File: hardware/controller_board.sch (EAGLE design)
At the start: 136 parts, among them J1 FRSKY-GIMBAL-FRYSKY, J11 USB-MICROA-AMPHENOL-10118192-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, J2 FRSKY-GIMBAL-FRYSKY, J3 USB-MINIB-EDAC-690-005-299-043, J4 AVR_SPI_PRG_6NS, J5 JUMPER-SMT_2_NC_PASTE_NO-SILK, J8 FRSKY-GIMBAL-2X-SERVO, J9 FRSKY-GIMBAL-2X-SERVO, P1 TEST-POINT, P2 TEST-POINT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

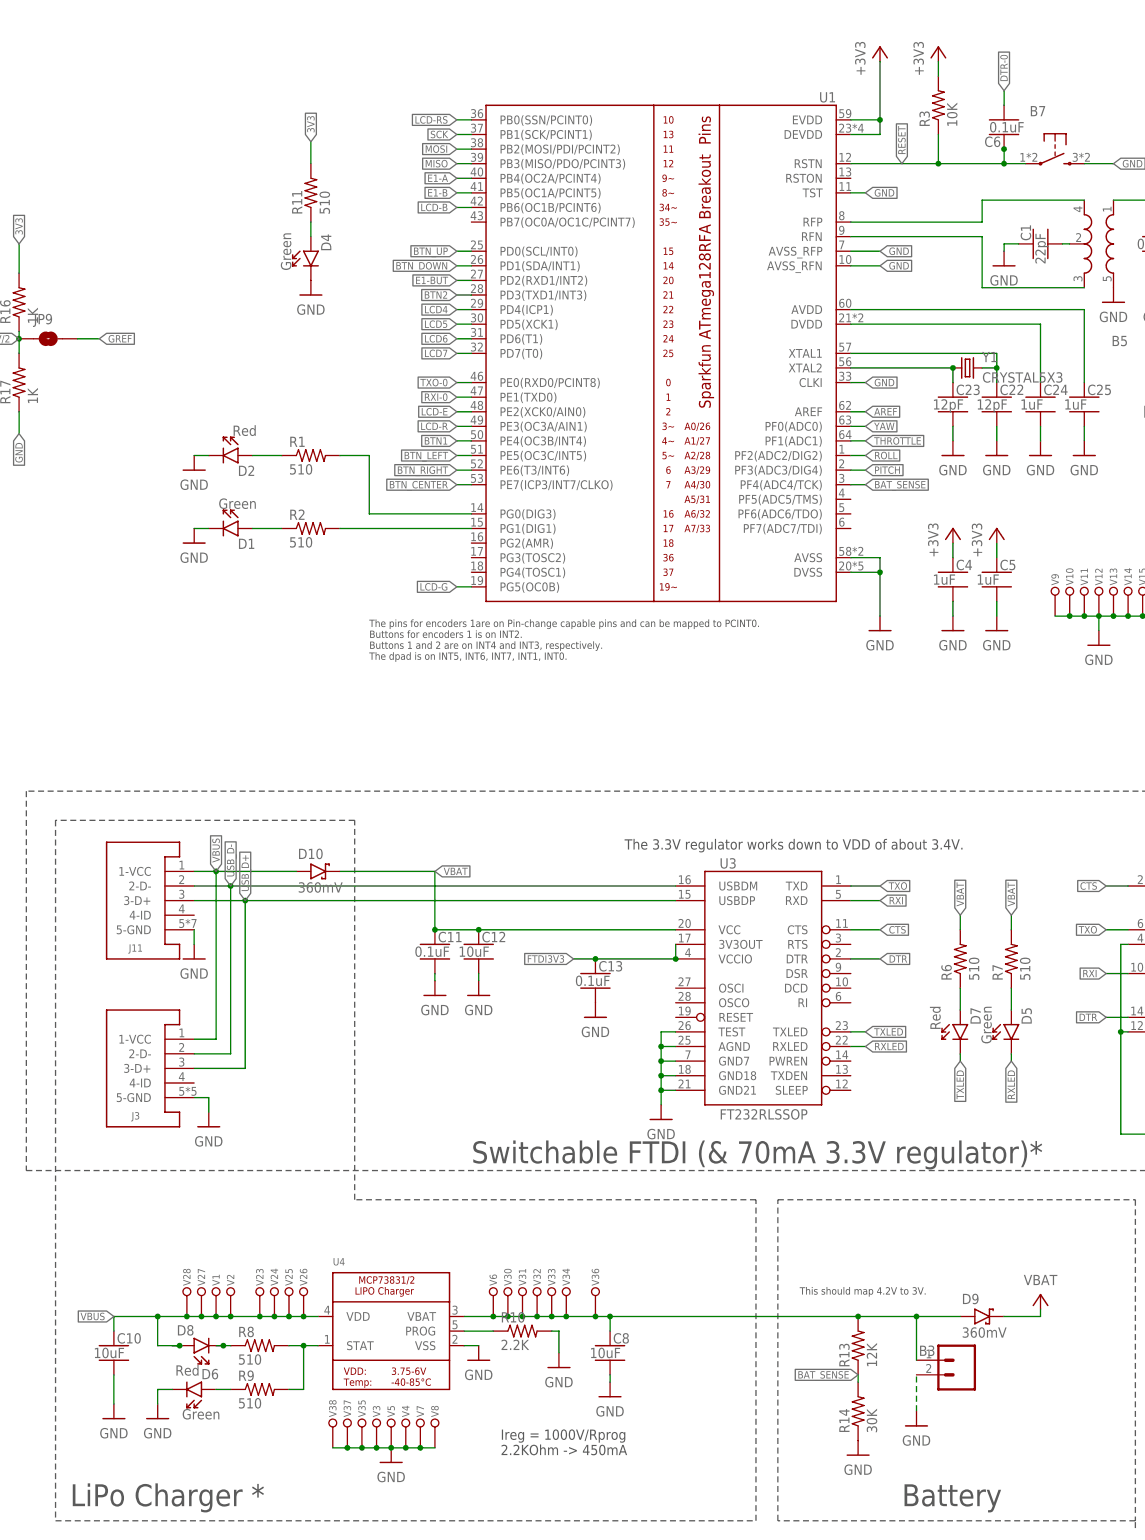
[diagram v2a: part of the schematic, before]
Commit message: moved everything to dual LEDs w/ shared resistors.
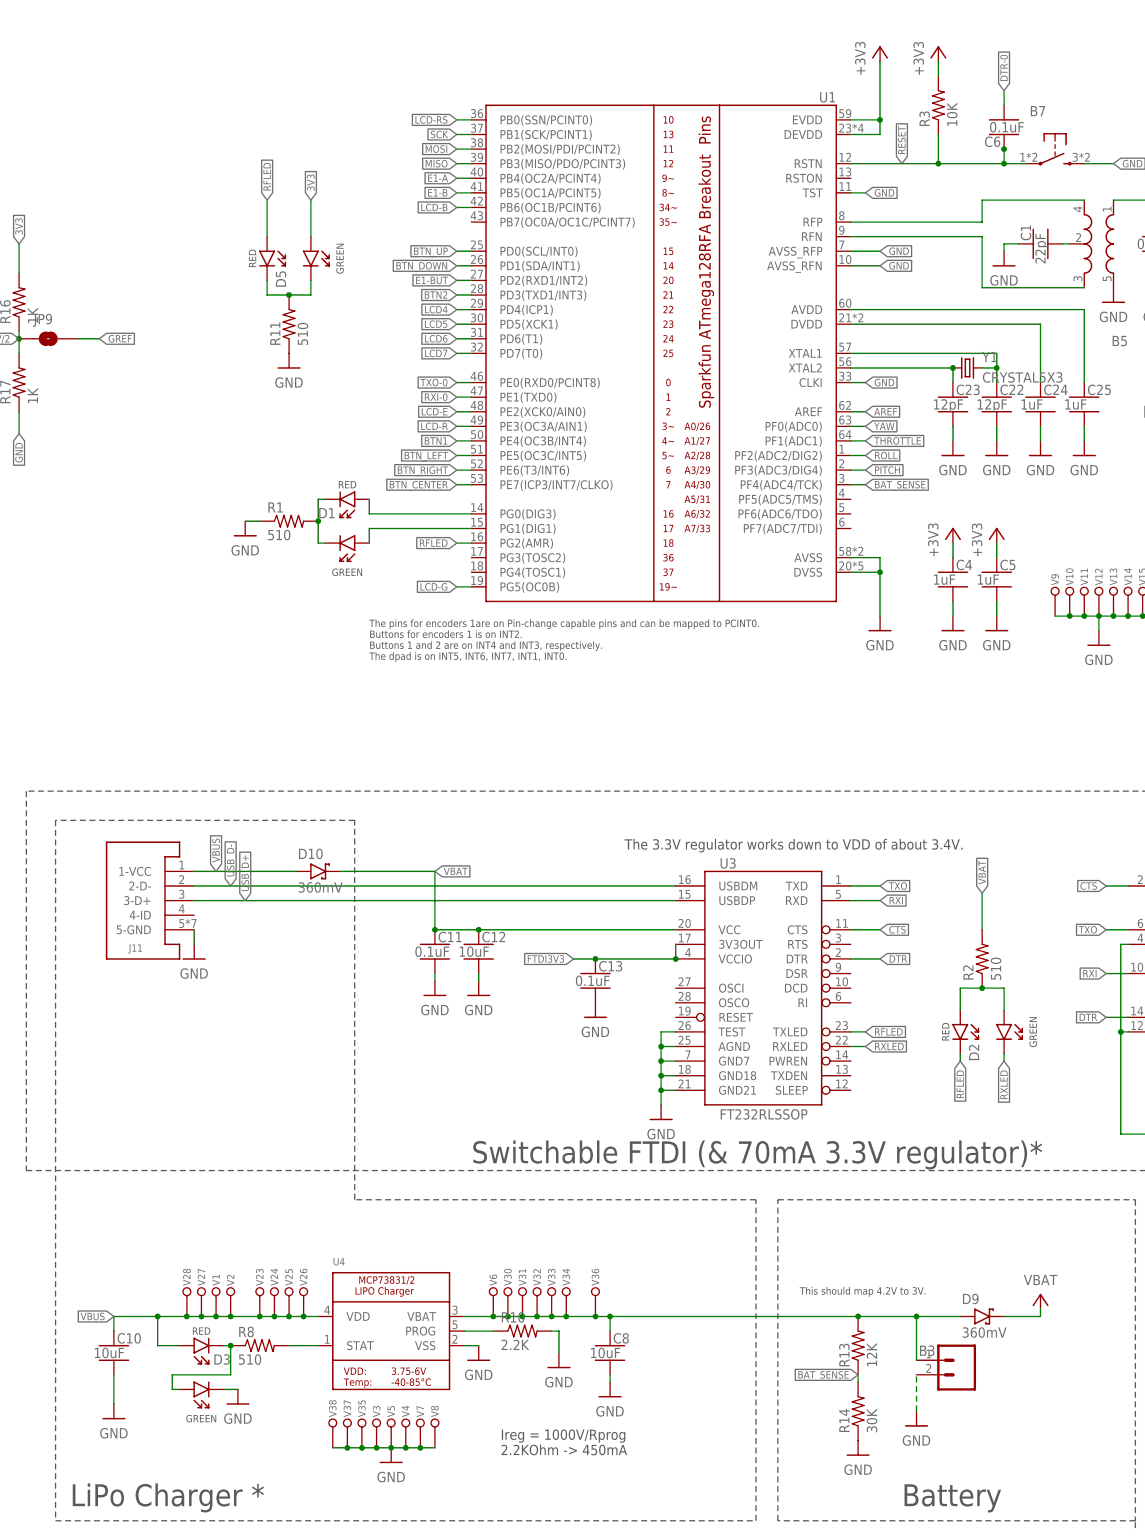
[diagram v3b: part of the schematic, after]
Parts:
- removed D4, D6: Green, RemoteParts:DIODE-LED_SMD-2012-0805-GREEN
- removed D7, D8: Red, RemoteParts:DIODE-LED_SMD-2012-0805-RED
- removed J3: USB-MINIB-EDAC-690-005-299-043, RemoteParts:USB-MINIB-EDAC-690-005-299-043
- removed R6, R7, R9: 510, quadparts_prebuilt:RESISTOR_SMD-2012-0805-510
- added D3: LED-2X-GREEN/RED, RemoteParts:LED-2X-GREEN/RED
- D1, D5: value Green -> LED-2X-GREEN/RED; device RemoteParts:DIODE-LED_SMD-2012-0805-GREEN -> RemoteParts:LED-2X-GREEN/RED
- D2: value Red -> LED-2X-GREEN/RED; device RemoteParts:DIODE-LED_SMD-2012-0805-RED -> RemoteParts:LED-2X-GREEN/RED
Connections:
- removed net N$10: D1.A, R2.1
- removed net N$13: D6.A, R9.1
- removed net N$14: D4.A, R11.1
- removed net TXLED: D7.C, U3.TXLED
- new net RFLED: D2.C2, D5.A2, U1.PG2(AMR), U3.TXLED
- net 3V3: no longer R11.2
- net GND: now also D3.C1, R1.1, R11.1; no longer D1.C, D2.C, D4.C, D6.C, J3.5-GND
- net N$11: no longer R9.2
- net N$2: now also D3.A1, D3.C2, R8.1; no longer D7.A, R6.1
- net N$3: now also D2.A1, D2.A2, R2.1; no longer D5.A, R7.1
- net N$4: now also D1.C1, D1.C2, R1.2; no longer R2.2, U1.PG1(DIG1)
- net N$6: now also D5.C1, D5.C2, R11.2; no longer D8.C, R8.1
- net N$8: now also D1.A2; no longer R1.2
- net N$9: now also D1.A1, U1.PG1(DIG1); no longer D2.A, R1.1
- net RXLED: now also D2.C1; no longer D5.C
- net USB_D+: no longer J3.3-D+
- net USB_D-: no longer J3.2-D-
- net VBAT: now also R2.2; no longer R6.2, R7.2
- net VBUS: now also D3.A2; no longer D8.A, J3.1-VCC
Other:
- moved on the sheet: R1, R11, R2

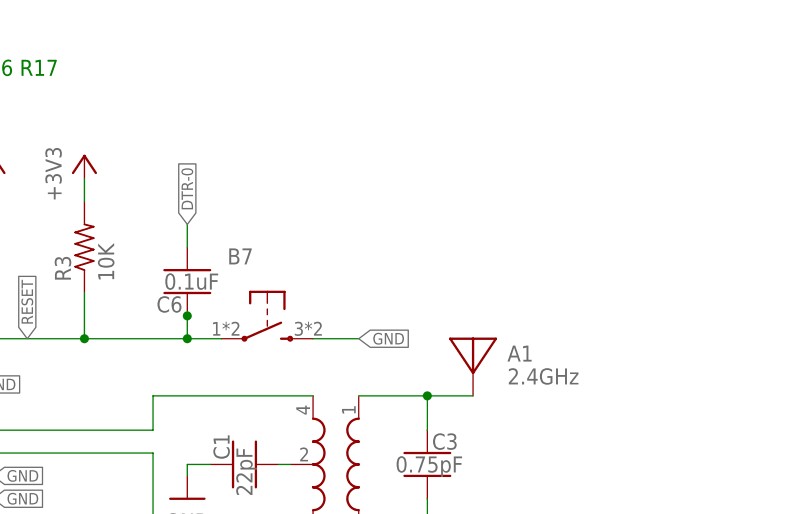
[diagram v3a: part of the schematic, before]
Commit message: note about using a bigger cap for the reset
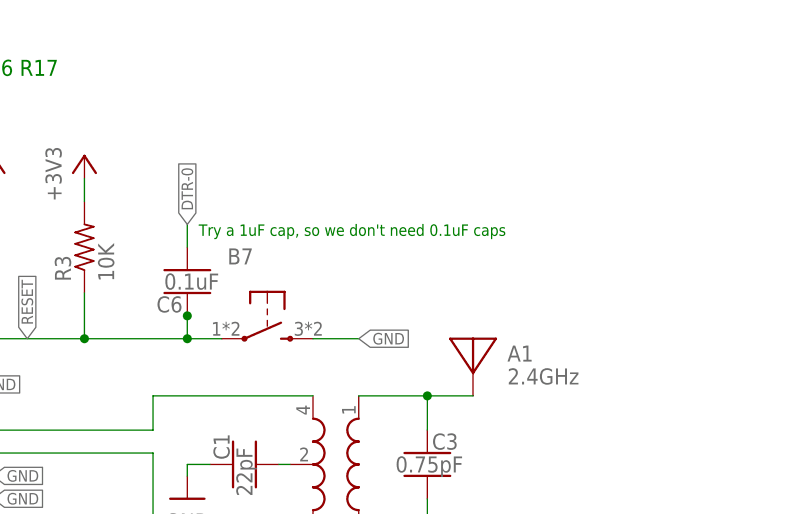
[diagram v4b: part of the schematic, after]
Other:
- note added: "Try a 1uF cap, so we don't need 0.1uF caps"
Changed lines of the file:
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@@
 <text x="87.63" y="269.24" size="1.778" layer="91">show  C11 C12 C13 R6 R7 D7 D5 U2 S2 S1 J1 J2 L1 P6 R15 R4 R5 R12 J11 J3 U3 P1 P2 P3 P4 B7 B2 B1 D8 R8 R9 D6 R13 r14 R16 R17</text>
 <text x="7.62" y="132.08" size="1.778" layer="97">C10 is the input cap (shared with lipo charger)</text>
+<text x="248.92" y="251.46" size="1.27" layer="91">Try a 1uF cap, so we don't need 0.1uF caps</text>
 </plain>
 <instances>

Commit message: part for new encoder
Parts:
- E1: value ROTARY-ENCODER-W/BUTTON-BOURNS-PEC12R-30MM -> ROTARY-ENCODER-W/BUTTON-BOURNS-PEC12R-4217F; device RemoteParts:ROTARY-ENCODER-W/BUTTON-BOURNS-PEC12R-30MM -> RemoteParts:ROTARY-ENCODER-W/BUTTON-BOURNS-PEC12R-4217F
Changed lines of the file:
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@@
 <setting verticaltext="up"/>
 </settings>
-<grid distance="0.05" unitdist="inch" unit="inch" style="lines" multiple="1" display="no" altdistance="0.01" altunitdist="inch" altunit="inch"/>
+<grid distance="0.1" unitdist="inch" unit="inch" style="lines" multiple="1" display="no" altdistance="0.01" altunitdist="inch" altunit="inch"/>
 <layers>
 <layer number="99" name="SpiceOrder" color="7" fill="1" visible="no" active="no"/>
@@
 <part name="B10" library="quadparts_prebuilt" deviceset="PUSHBUTTON_" device="-4.5X4.5" value="PUSHBUTTON_-4.5X4.5"/>
 <part name="JP7" library="RemoteParts" deviceset="JUMPER-SMT_3_1-NC_PASTE" device="_NO-SILK"/>
-<part name="E1" library="RemoteParts" deviceset="ROTARY-ENCODER-W/BUTTON" device="-BOURNS-PEC12R-30MM"/>
+<part name="E1" library="RemoteParts" deviceset="ROTARY-ENCODER-W/BUTTON" device="-BOURNS-PEC12R-4217F"/>
 <part name="J5" library="RemoteParts" deviceset="JUMPER-SMT_2_NC_PASTE" device="_NO-SILK"/>
 <part name="JP6" library="RemoteParts" deviceset="JUMPER-SMT_3_1-NC_PASTE" device="_NO-SILK"/>

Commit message: handrouting done
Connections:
- net USB_D+ renamed USB_D_P
- net USB_D- renamed USB_D_N
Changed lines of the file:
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@@
 </segment>
 </net>
-<net name="USB_D-" class="0">
+<net name="USB_D_N" class="0">
 <segment>
 <wire x1="190.5" y1="114.3" x2="106.68" y2="114.3" width="0.1524" layer="91"/>
@@
 </segment>
 </net>
-<net name="USB_D+" class="0">
+<net name="USB_D_P" class="0">
 <segment>
 <wire x1="190.5" y1="111.76" x2="106.68" y2="111.76" width="0.1524" layer="91"/>

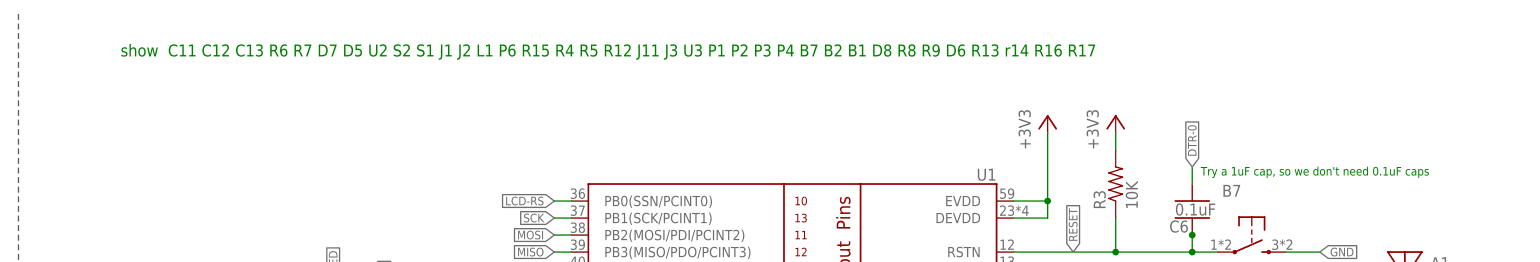
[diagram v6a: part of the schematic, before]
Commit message: define assembly variants
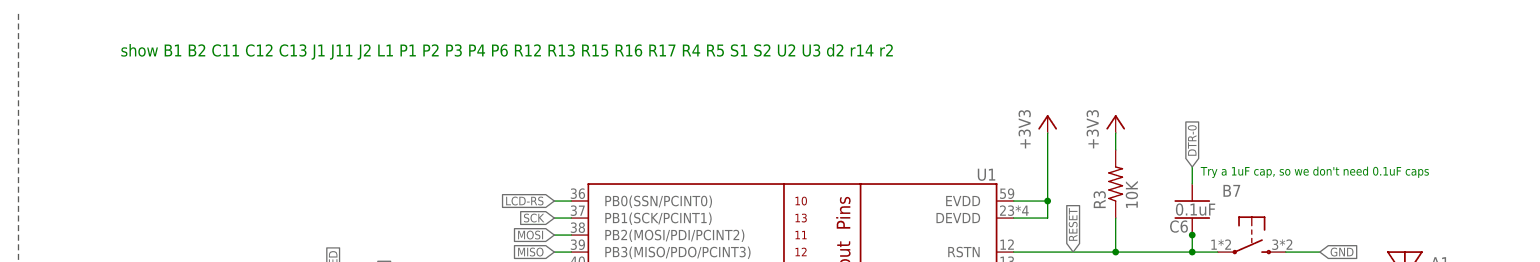
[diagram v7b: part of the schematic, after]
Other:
- note added: "show B1 B2 C11 C12 C13 J1 J11 J2 L1 P1 P2 P3 P4 P6 R12 R13 R15 R16 R17 R4 R5 S1 S2 U2 U3 d2 r14 r2"
- note removed: "show C11 C12 C13 R6 R7 D7 D5 U2 S2 S1 J1 J2 L1 P6 R15 R4 R5 R12 J11 J3 U3 P1 P2 P3 P4 B7 B2 B1 D8 R8 R9 D6 R13 r14 R16 R17"

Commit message: connect PWR led to power
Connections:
- net 3V3: now also D5.A1
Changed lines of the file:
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@@
 <variantdefs>
 <variantdef name="Minimal"/>
-<variantdef name="FullAwesome" current="yes"/>
+<variantdef name="FullAwesome"/>
 </variantdefs>
 <classes>
@@
 <label x="127" y="233.68" size="1.27" layer="95" rot="R90" xref="yes"/>
 <wire x1="127" y1="227.33" x2="127" y2="233.68" width="0.1524" layer="91"/>
-</segment>
-<segment>
+<pinref part="D5" gate="G$1" pin="A1"/>
+</segment>
+<segment>
